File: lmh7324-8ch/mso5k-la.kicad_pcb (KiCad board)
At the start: 4 copper layers, 40 x 42 mm, 101 parts, among them IC201 lmh7324, IC401 lmh7324, J101 out, J102 in, J103 3mm, J104 3mm, J105 3mm, J106 3mm, U401 ATtiny85-20SU

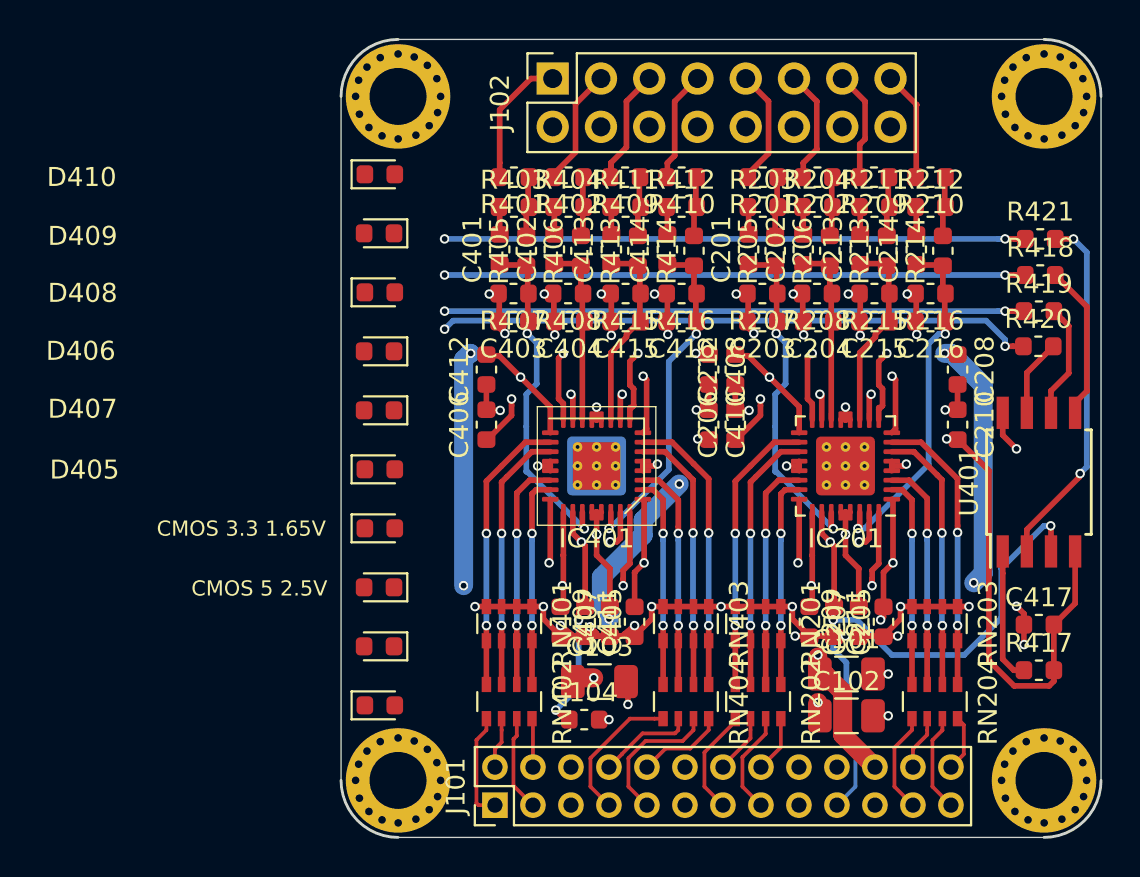
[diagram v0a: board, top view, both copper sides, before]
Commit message: Completed lmh7324 based 8ch pod with voltmeter
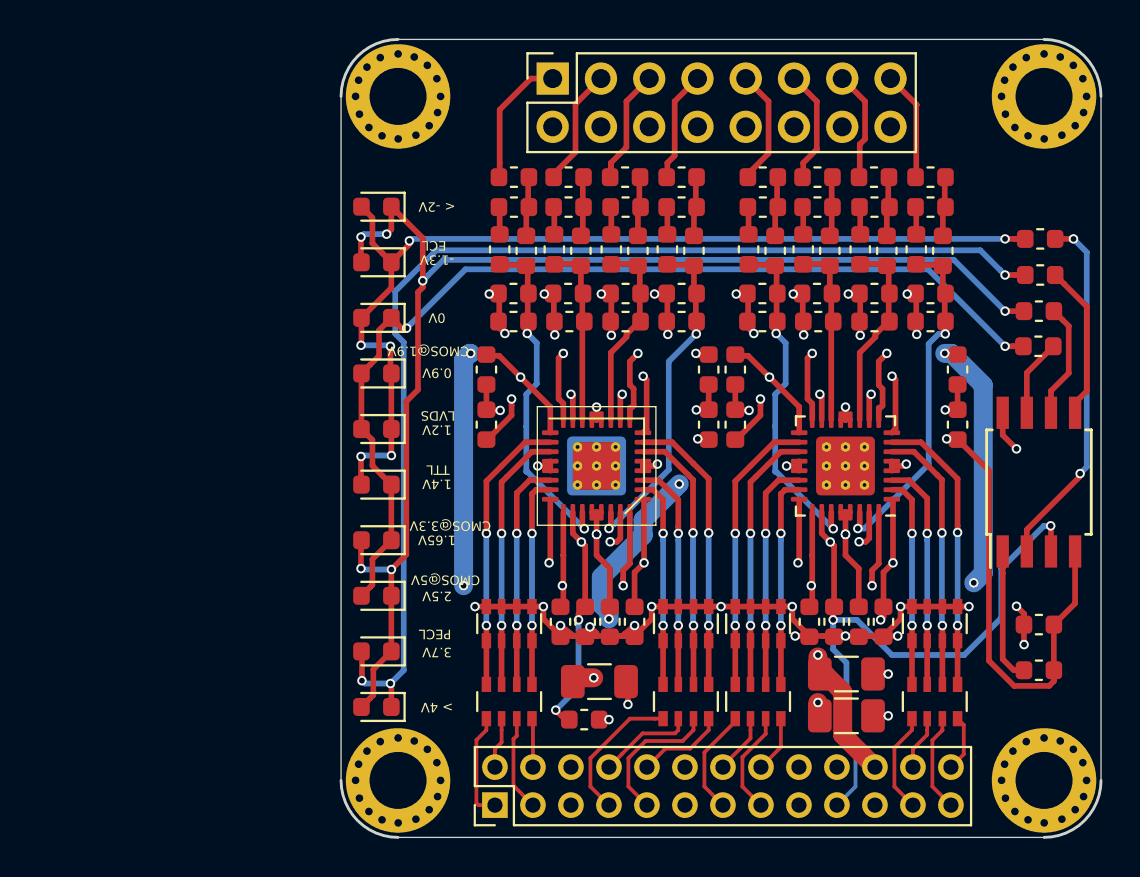
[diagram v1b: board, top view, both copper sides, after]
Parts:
- moved D406 4.09 mm to (46.9, 165.5)
- moved D407 1.95 mm to (46.9, 162.6)
- moved D410 1.71 mm to (46.9, 153.8), turned to 180 degrees
- moved D409 1.53 mm to (46.9, 156.7)
- moved D408 1.36 mm to (46.9, 159.7), turned to 180 degrees
- moved D405 0.82 mm to (46.9, 168.4), turned to 180 degrees
- moved D404 0.65 mm to (46.9, 171.4), turned to 180 degrees
- moved D403 0.47 mm to (46.9, 174.3)
- moved D402 0.30 mm to (46.9, 177.2)
- moved D401 0.20 mm to (46.9, 180.1), turned to 180 degrees
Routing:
- net Net-(D401-Pad2): track 30.5 -> 69.0 mm, vias 2 -> 6
- net Net-(D401-Pad1): track 30.6 -> 60.1 mm, vias 2 -> 3
- net Net-(D405-Pad2): track 30.6 -> 53.0 mm, vias 2 -> 6
- net Net-(D403-Pad2): track 31.4 -> 53.0 mm
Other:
- board text added: "-1.3V"
- board text added: "0.9V"
- board text added: "0V"
- board text added: "1.2V"
- board text added: "1.4V"
- board text added: "1.65V"
- board text added: "2.5V"
- board text added: "3.7V"
- board text added: "< -2V"
- board text added: "> 4V"
- board text added: "CMOS@1.9V"
- board text added: "CMOS@3.3V"
- board text added: "CMOS@5V"
- board text added: "ECL"
- board text added: "LVDS"
- board text added: "PECL"
- board text added: "TTL"

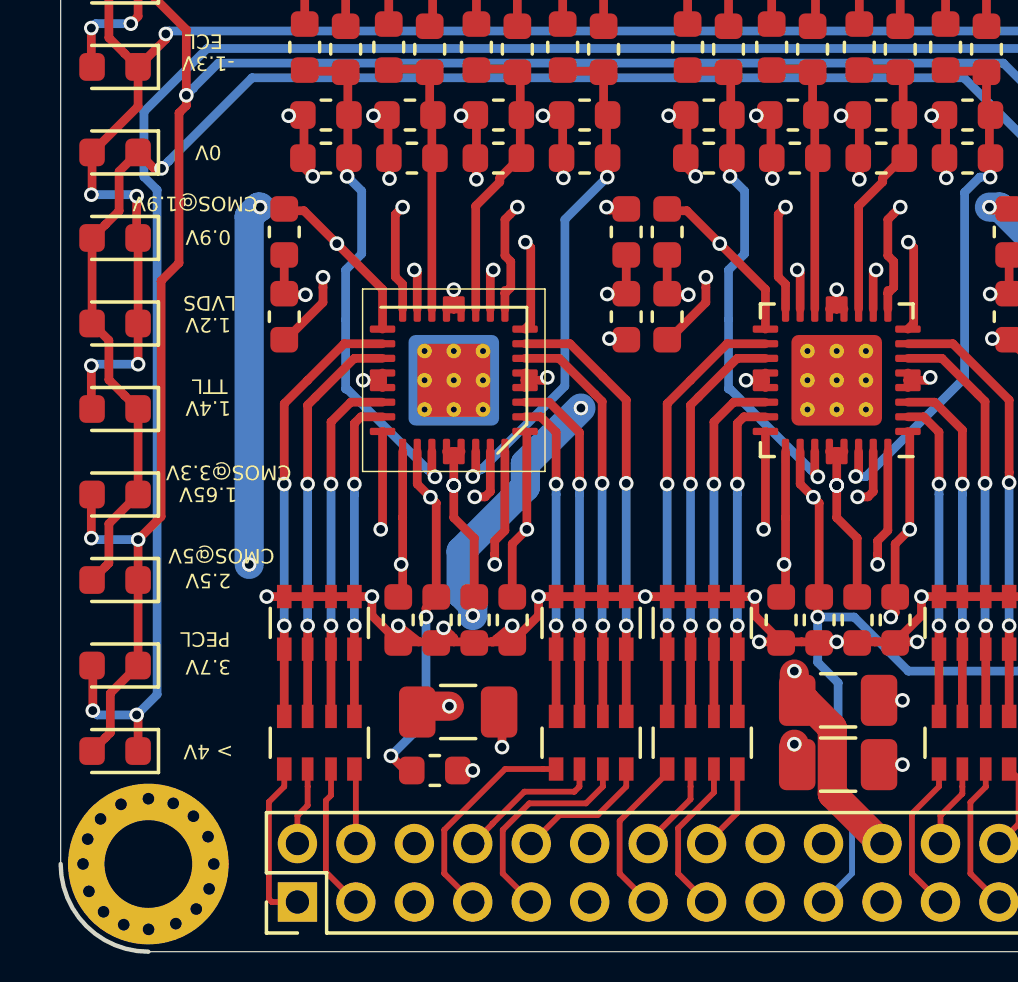
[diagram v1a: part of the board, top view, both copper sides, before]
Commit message: Golden revision before switching to SMD 1.27mm pitch header
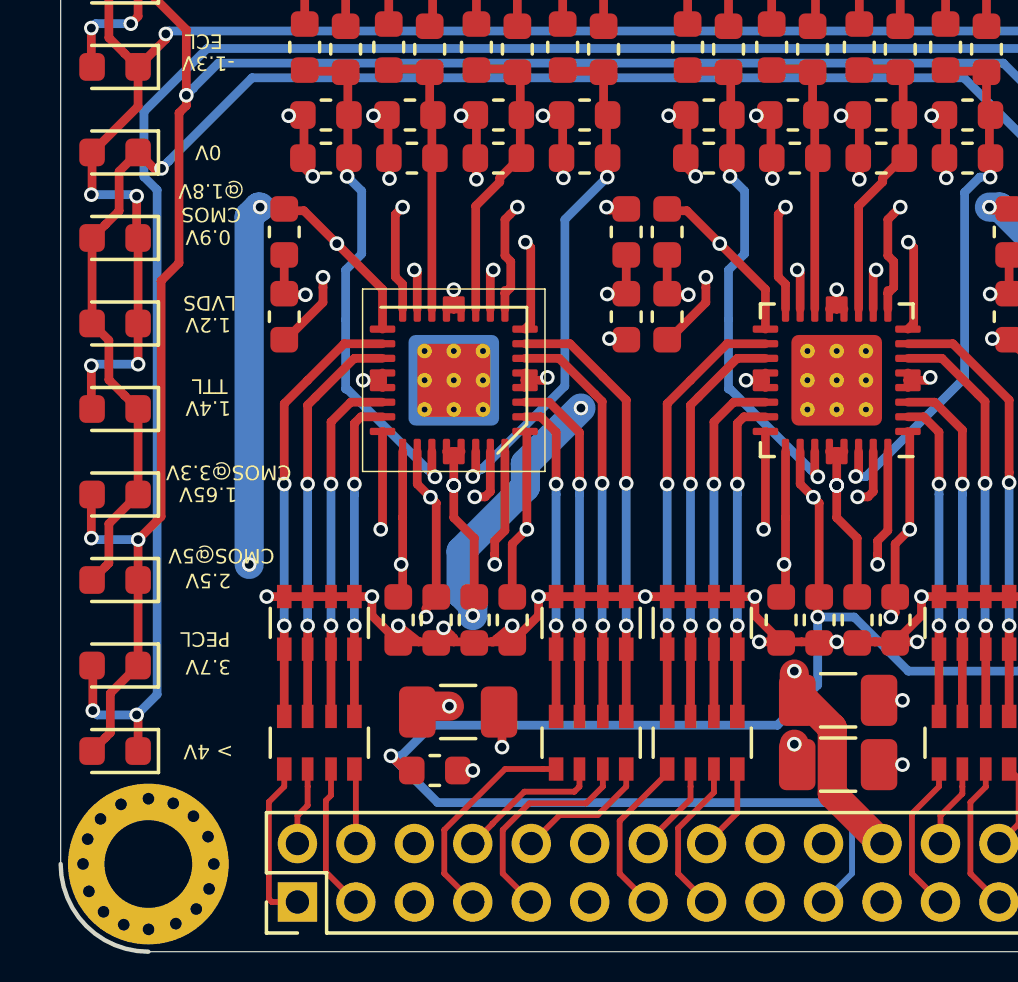
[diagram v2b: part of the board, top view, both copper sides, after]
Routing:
- net Vref: track 131.5 -> 153.5 mm
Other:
- board text added: "CMOS @1.8V"
- board text removed: "CMOS@1.9V"
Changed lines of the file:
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@@
     (thickness 1.6)
     (drawings 32)
-    (tracks 1166)
+    (tracks 1168)
     (zones 0)
     (modules 101)
@@
       (effects (font (size 0.5 0.5) (thickness 0.083333)))
     )
-    (fp_text user %R (at -0.14 -0.45 180) (layer F.Fab)
+    (fp_text user %R (at 0.011713 0.004181 180) (layer F.Fab)
       (effects (font (size 0.4 0.4) (thickness 0.06)))
     )
@@
     (effects (font (size 0.5 0.5) (thickness 0.125)))
   )
-  (gr_text CMOS@1.9V (at 49.6 161.4 180) (layer F.SilkS)
+  (gr_text "CMOS\n@1.8V" (at 50.15 161.375 180) (layer F.SilkS)
     (effects (font (size 0.5 0.5) (thickness 0.125)))
   )
@@
     (arrow2b (pts (xy 88 145) (xy 88.586421 146.126504)))
   )
-  (dimension 41 (width 0.3) (layer F.Fab)
-    (gr_text "41.000 mm" (at 65.5 140.9) (layer F.Fab)
+  (dimension 40 (width 0.3) (layer F.Fab)
+    (gr_text "40.000 mm" (at 65 140.9) (layer F.Fab)
       (effects (font (size 1.5 1.5) (thickness 0.3)))
     )
-    (feature1 (pts (xy 86 145) (xy 86 142.413579)))
+    (feature1 (pts (xy 85 145) (xy 85 142.413579)))
     (feature2 (pts (xy 45 145) (xy 45 142.413579)))
-    (crossbar (pts (xy 45 143) (xy 86 143)))
-    (arrow1a (pts (xy 86 143) (xy 84.873496 143.586421)))
-    (arrow1b (pts (xy 86 143) (xy 84.873496 142.413579)))
+    (crossbar (pts (xy 45 143) (xy 85 143)))
+    (arrow1a (pts (xy 85 143) (xy 83.873496 143.586421)))
+    (arrow1b (pts (xy 85 143) (xy 83.873496 142.413579)))
     (arrow2a (pts (xy 45 143) (xy 46.126504 143.586421)))
     (arrow2b (pts (xy 45 143) (xy 46.126504 142.413579)))
@@
   (segment (start 71.1 185.3) (end 72.075001 184.324999) (width 0.2) (layer B.Cu) (net 69) (status 10))
   (segment (start 72.075001 182.375001) (end 71.6 181.9) (width 0.2) (layer B.Cu) (net 69))
-  (segment (start 71.6 181.9) (end 71.6 177.8) (width 0.3) (layer B.Cu) (net 69))
   (via (at 70.9 175.549998) (size 0.5) (drill 0.3) (layers F.Cu B.Cu) (net 69))
-  (segment (start 71.6 177.8) (end 70.9 177.1) (width 0.3) (layer B.Cu) (net 69))
-  (segment (start 70.9 177.1) (end 70.9 175.549998) (width 0.3) (layer B.Cu) (net 69))
   (segment (start 70.9 174.95) (end 70.95 174.9) (width 0.3) (layer F.Cu) (net 69) (status 30))
   (segment (start 70.9 175.549998) (end 70.9 174.95) (width 0.3) (layer F.Cu) (net 69) (status 20))
@@
   (segment (start 56.8 180.8) (end 56.3 180.3) (width 0.3) (layer F.Cu) (net 69) (status 10))
   (via (at 57.5 175.549998) (size 0.5) (drill 0.3) (layers F.Cu B.Cu) (net 69))
-  (segment (start 56.3 180.3) (end 57.5 179.1) (width 0.3) (layer B.Cu) (net 69))
-  (segment (start 57.5 179.1) (end 57.5 175.549998) (width 0.3) (layer B.Cu) (net 69))
   (segment (start 57.5 175.25) (end 57.85 174.9) (width 0.3) (layer F.Cu) (net 69) (status 30))
   (segment (start 57.5 175.549998) (end 57.5 175.25) (width 0.3) (layer F.Cu) (net 69) (status 20))
@@
   (segment (start 72.149998 175.549998) (end 70.9 175.549998) (width 0.3) (layer B.Cu) (net 69))
   (segment (start 74 177.4) (end 72.149998 175.549998) (width 0.3) (layer B.Cu) (net 69))
+  (segment (start 57.9 181.9) (end 56.3 180.3) (width 0.3) (layer B.Cu) (net 69))
+  (segment (start 71.6 181.9) (end 57.9 181.9) (width 0.3) (layer B.Cu) (net 69))
+  (segment (start 56.653553 180.3) (end 57.703553 179.25) (width 0.3) (layer B.Cu) (net 69))
+  (segment (start 56.3 180.3) (end 56.653553 180.3) (width 0.3) (layer B.Cu) (net 69))
+  (segment (start 57.703553 179.25) (end 69.525 179.25) (width 0.3) (layer B.Cu) (net 69))
+  (segment (start 70.9 177.875) (end 70.9 175.549998) (width 0.3) (layer B.Cu) (net 69))
+  (segment (start 69.525 179.25) (end 70.9 177.875) (width 0.3) (layer B.Cu) (net 69))
   (segment (start 80.9425 159.3) (end 79.95 159.3) (width 0.3) (layer F.Cu) (net 70) (status 10))
   (via (at 79.95 159.3) (size 0.5) (drill 0.3) (layers F.Cu B.Cu) (net 70))
